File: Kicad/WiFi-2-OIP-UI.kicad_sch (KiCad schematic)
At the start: 10 parts, among them J2 Phoenix contact 1803277 + 185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, J201 2x 1x05 pin header 2.54mm, J202 MountingHole_Pad, U1 LM7805 buck module

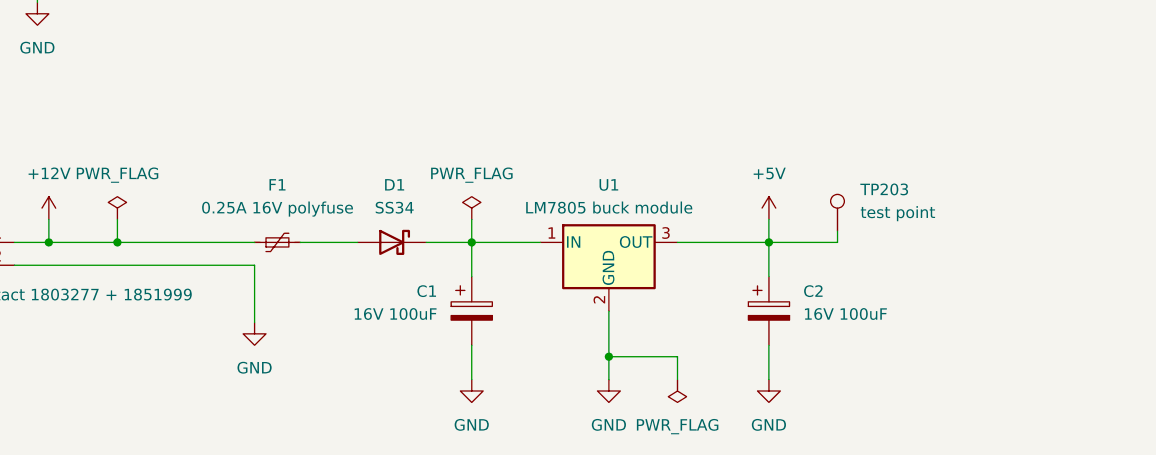
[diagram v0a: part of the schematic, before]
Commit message: Change fuse to 0.2A
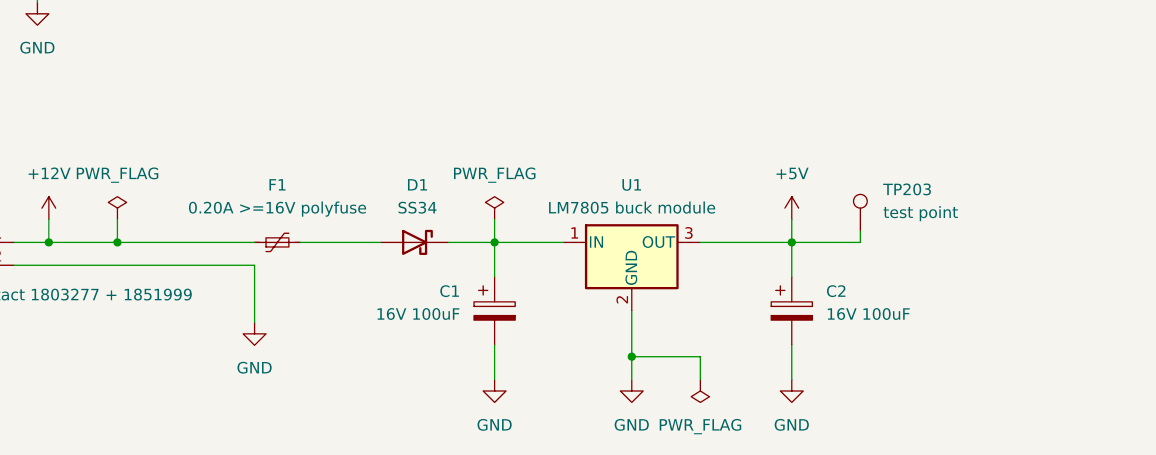
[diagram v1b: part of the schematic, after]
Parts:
- F1: value 0.25A 16V polyfuse -> 0.20A >=16V polyfuse
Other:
- moved on the sheet: C1, C2, D1, TP203, U1
